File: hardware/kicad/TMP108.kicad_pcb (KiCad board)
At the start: 2 copper layers, 75 x 75 mm, 38 parts, among them J1 Screw_Terminal_01x08, J2 Screw_Terminal_01x08, J3 CAN, SW1 PRG, SW2 BUS, SW3 PRG-VALUE, U1 Teensy_3.2, U2 TMR-1211, U3 MCP2551-I-P

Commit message: PCB parts list, etc.
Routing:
- net Net-(R15-Pad2): track 0.25 -> 3.56 mm

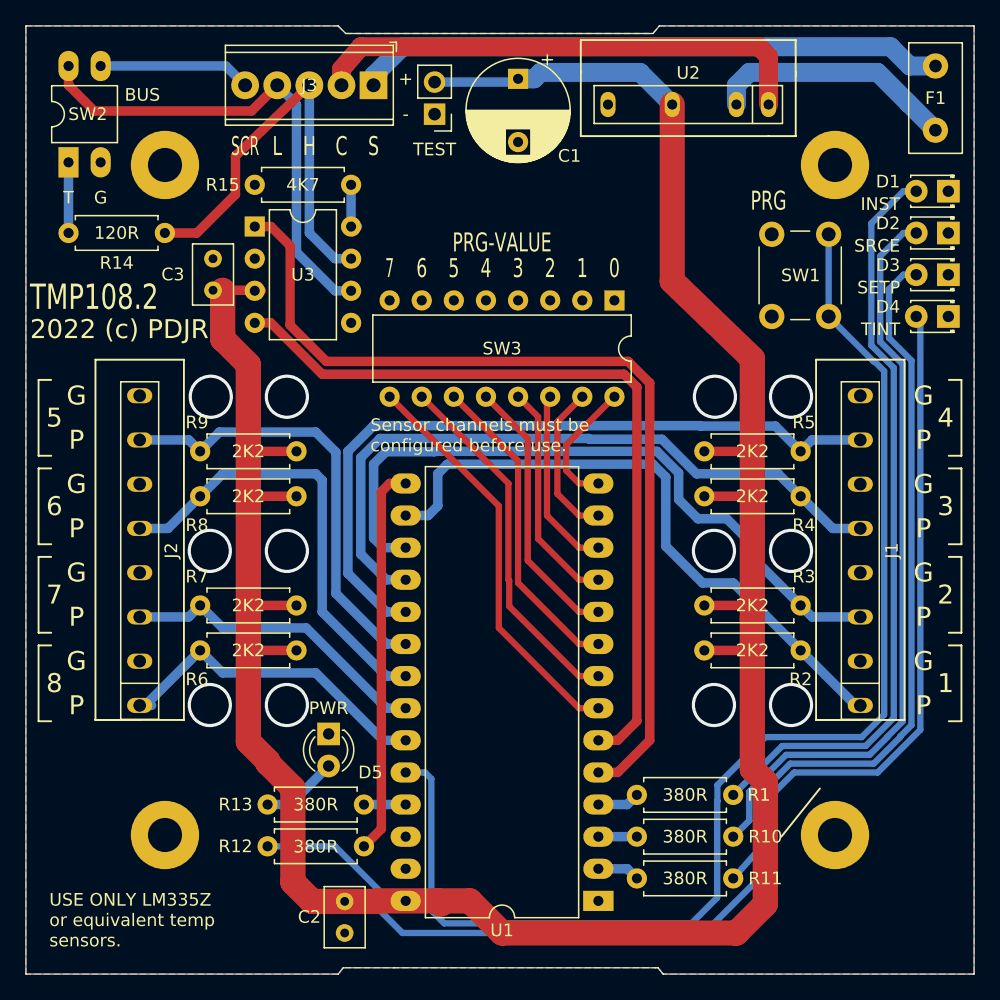
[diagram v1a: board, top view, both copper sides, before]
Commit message: Increase PCB notch size.
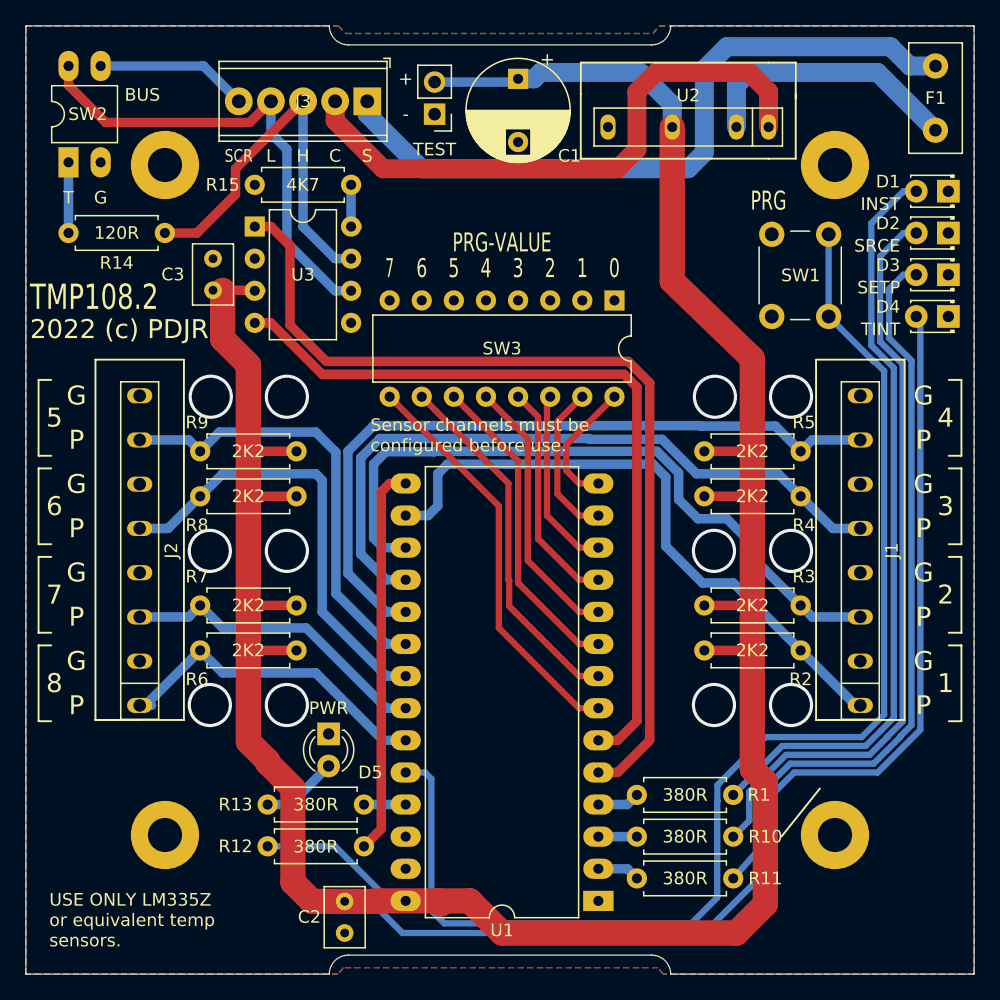
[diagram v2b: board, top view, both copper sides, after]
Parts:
- moved U2 1.78 mm to (188.4, 95.0)
- moved J3 1.36 mm to (163.0, 93.0)
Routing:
- net /NET_S: track 46.1 -> 56.3 mm
- net /NET_C: track 39.3 -> 46.7 mm
- net /CAN_H: track 33.8 -> 31.2 mm
- net Net-(F1-Pad2): track 19.6 -> 21.4 mm
- net /CAN_L: track 39.1 -> 37.8 mm
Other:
- outline, holes or cut-outs redrawn
